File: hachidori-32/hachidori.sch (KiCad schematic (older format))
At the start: 38 parts, among them P1 VIN, P2 UART, P4 I2C, SW1 FLASH, SW2 RESET, U1 NCP1117ST33, U2 MPU-9250, U4 BME280, U7 INA226

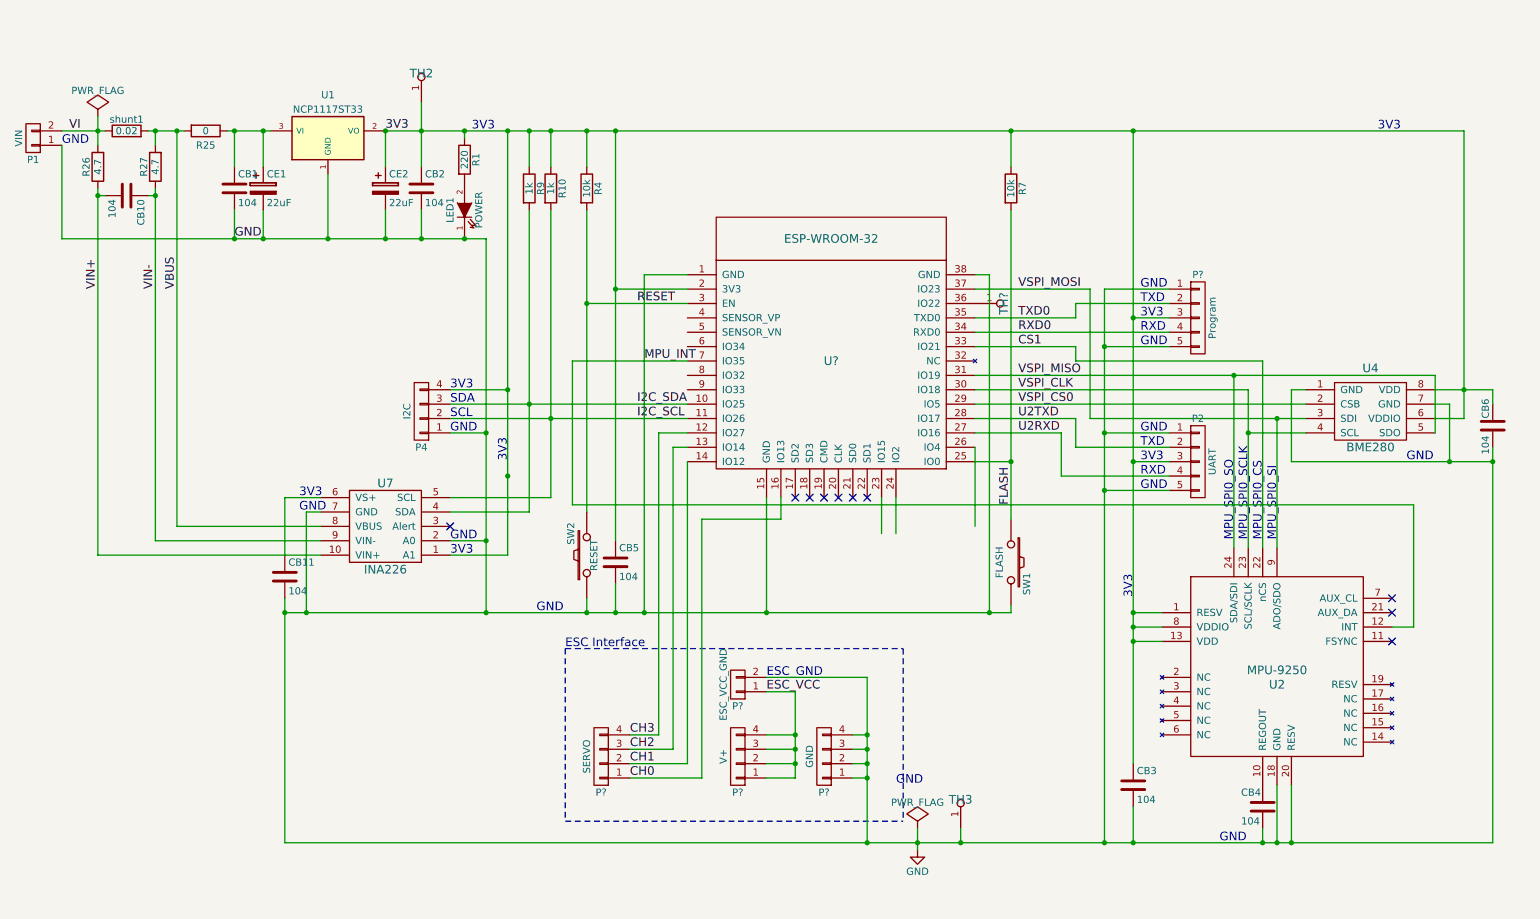
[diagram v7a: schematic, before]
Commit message: Add RGB LED
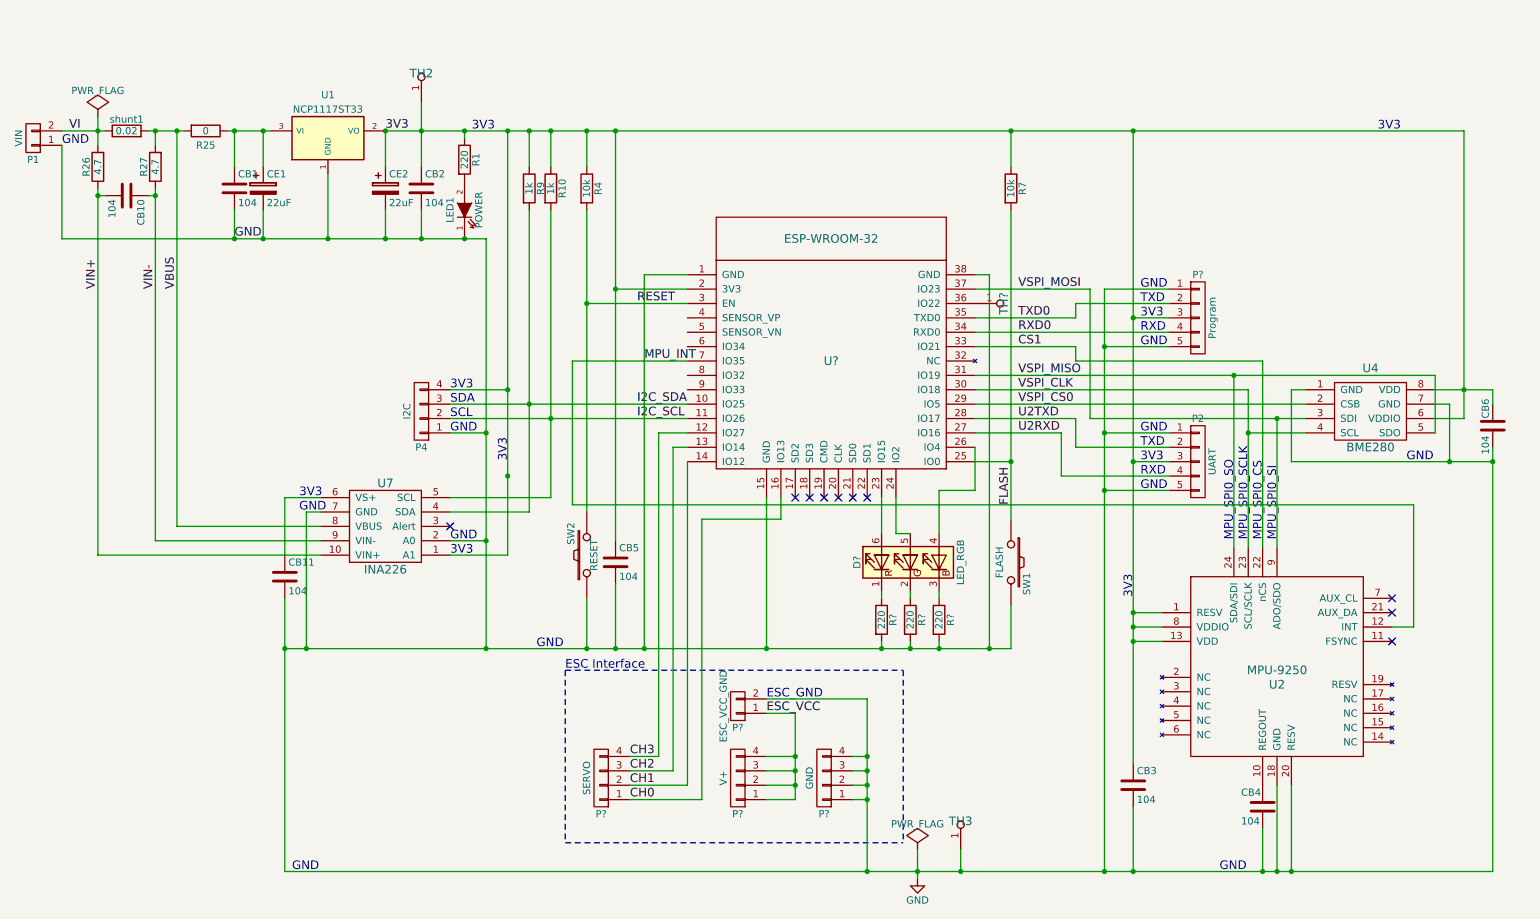
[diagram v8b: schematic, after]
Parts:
- added D?: LED_RGB, symbol LED_RGB
- added R? (x3): 220, rohm:MCR03, symbol R
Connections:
- net GND: now also R?.2, R?.2, R?.2
- net at U?.23 (IO15): now also D?.6 (RA)
- net at U?.24 (IO2): now also D?.5 (GA)
- net at U?.26 (IO4): now also D?.4 (BA)
- new net: D?.1 (RK), R?.1
- new net: D?.2 (GK), R?.1
- new net: D?.3 (BK), R?.1
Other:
- moved on the sheet: P?, TH3
